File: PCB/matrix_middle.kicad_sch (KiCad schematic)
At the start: 70 parts, among them J12 Conn_02x02_Top_Bottom, J13 Conn_02x02_Top_Bottom, J14 Conn_02x02_Top_Bottom

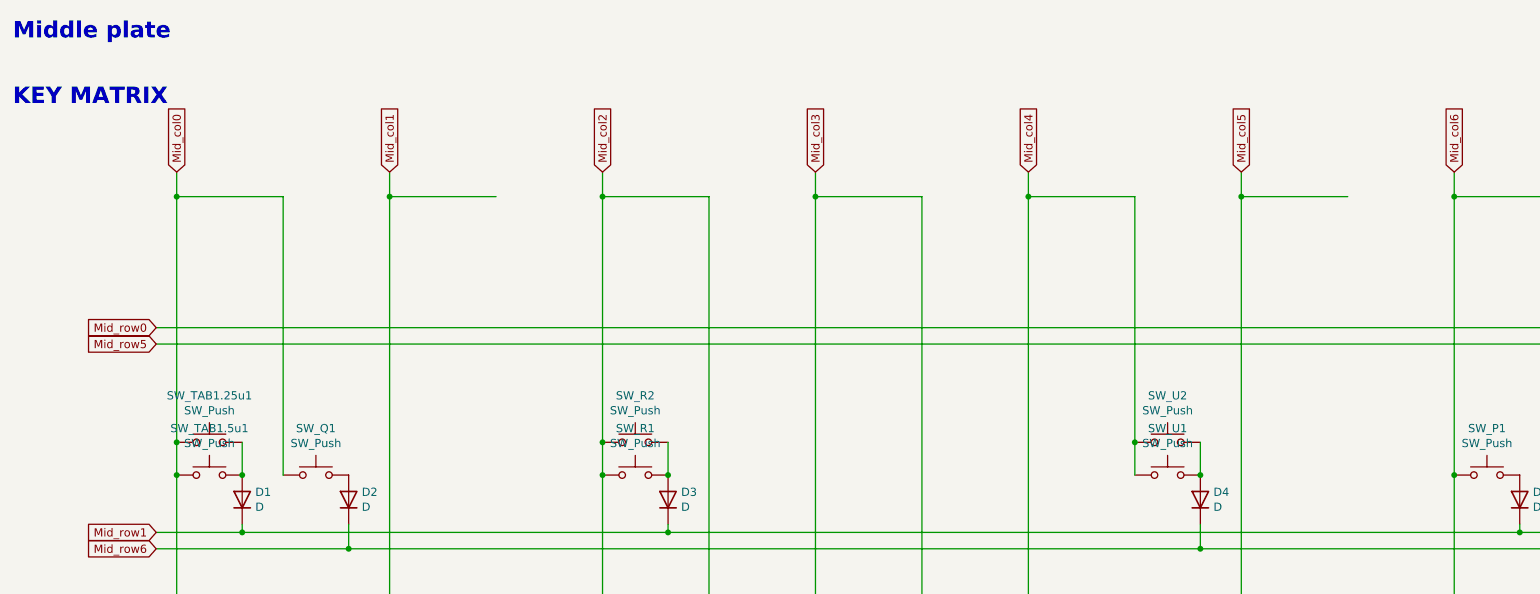
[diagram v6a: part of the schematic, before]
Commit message: スイッチのソケットを廃止
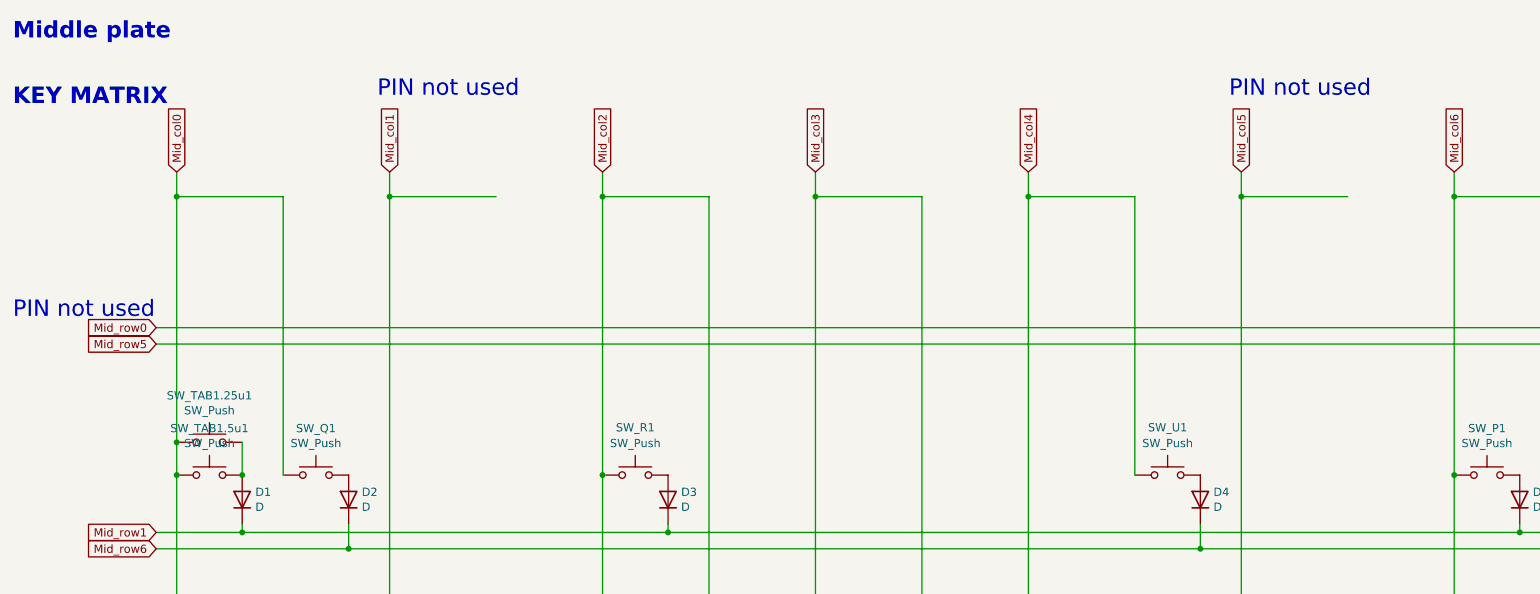
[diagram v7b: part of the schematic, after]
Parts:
- removed SW_R2, SW_U2: SW_Push, MX_Alps_Hybrid:MXOnly-1U-NoLED, symbol Switch:SW_Push
- SW_'1, SW_;2, SW_G1, SW_H1, SW_P1, SW_Q1, SW_R1, SW_R4CenterC1, SW_R4CenterL1, SW_R4CenterR1, SW_U1: footprint MX_Alps_Hybrid:MXOnly-1U-Hotswap-guide -> MX_Alps_Hybrid:MXOnly-1U-NoLED
- SW_BS1.5u1, SW_TAB1.5u1: footprint MX_Alps_Hybrid:MXOnly-1.5U-Hotswap-guide -> MX_Alps_Hybrid:MXOnly-1.5U-NoLED
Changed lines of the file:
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@@
   (junction (at 246.38 93.98) (diameter 0) (color 0 0 0 0)
   )
-  (junction (at 196.85 85.09) (diameter 0) (color 0 0 0 0)
-  )
   (junction (at 211.455 273.05) (diameter 0) (color 0 0 0 0)
   )
-  (junction (at 186.69 80.01) (diameter 0) (color 0 0 0 0)
-  )
   (junction (at 180.34 125.73) (diameter 0) (color 0 0 0 0)
   )
@@
   (junction (at 163.83 160.02) (diameter 0) (color 0 0 0 0)
   )
-  (junction (at 104.14 80.01) (diameter 0) (color 0 0 0 0)
-  )
   (junction (at 236.22 41.91) (diameter 0) (color 0 0 0 0)
   )
@@
   (junction (at 262.89 96.52) (diameter 0) (color 0 0 0 0)
   )
-  (junction (at 114.3 85.09) (diameter 0) (color 0 0 0 0)
-  )
   (wire (pts (xy 281.94 213.36) (xy 281.94 193.04))
     (stroke (width 0) (type default) (color 0 0 0 0))
@@
     (stroke (width 0) (type default) (color 0 0 0 0))
   )
-  (wire (pts (xy 104.14 80.01) (xy 104.14 85.09))
-    (stroke (width 0) (type default) (color 0 0 0 0))
-  )
   (wire (pts (xy 279.4 96.52) (xy 262.89 96.52))
     (stroke (width 0) (type default) (color 0 0 0 0))
@@
     (stroke (width 0) (type default) (color 0 0 0 0))
   )
-  (wire (pts (xy 104.14 41.91) (xy 104.14 80.01))
+  (wire (pts (xy 104.14 41.91) (xy 104.14 85.09))
     (stroke (width 0) (type default) (color 0 0 0 0))
   )
@@
     (stroke (width 0) (type default) (color 0 0 0 0))
   )
-  (wire (pts (xy 186.69 41.91) (xy 186.69 80.01))
-    (stroke (width 0) (type default) (color 0 0 0 0))
-  )
   (wire (pts (xy 220.345 247.65) (xy 186.055 247.65))
     (stroke (width 0) (type default) (color 0 0 0 0))
@@
     (stroke (width 0) (type default) (color 0 0 0 0))
   )
-  (wire (pts (xy 196.85 80.01) (xy 196.85 85.09))
-    (stroke (width 0) (type default) (color 0 0 0 0))
-  )
   (wire (pts (xy 64.77 96.52) (xy 196.85 96.52))
     (stroke (width 0) (type default) (color 0 0 0 0))
@@
     (stroke (width 0) (type default) (color 0 0 0 0))
   )
-  (wire (pts (xy 186.69 80.01) (xy 186.69 85.09))
+  (wire (pts (xy 186.69 41.91) (xy 186.69 85.09))
     (stroke (width 0) (type default) (color 0 0 0 0))
   )
@@
     (stroke (width 0) (type default) (color 0 0 0 0))
   )
-  (wire (pts (xy 114.3 80.01) (xy 114.3 85.09))
-    (stroke (width 0) (type default) (color 0 0 0 0))
-  )
   (wire (pts (xy 196.85 96.52) (xy 262.89 96.52))
     (stroke (width 0) (type default) (color 0 0 0 0))
@@
   (wire (pts (xy 71.12 38.1) (xy 71.12 41.91))
     (stroke (width 0) (type default) (color 0 0 0 0))
+  )
+  (text "PIN not used" (at 69.215 26.67 0)
+    (effects (font (size 2.54 2.54)) (justify left bottom))
   )
   (text "5-way navigation switch" (at 228.6 177.8 0)
@@
     (effects (font (size 2.54 2.54)) (justify left bottom))
   )
+  (text "PIN not used" (at 201.295 26.67 0)
+    (effects (font (size 2.54 2.54)) (justify left bottom))
+  )
   (text "Bottom to Mid: require 12 pins" (at 21.59 222.25 0)
     (effects (font (size 5.08 5.08) (thickness 1.016) bold) (justify left bottom))
@@
   (text "SCREWS to Bottom" (at 187.96 231.14 0)
     (effects (font (size 2.54 2.54) (thickness 0.508) bold) (justify left bottom))
+  )
+  (text "PIN not used" (at 12.7 60.96 0)
+    (effects (font (size 2.54 2.54)) (justify left bottom))
   )
   (global_label "Mid_col5" (shape input) (at 203.2 38.1 90) (fields_autoplaced)
@@
     (pin "1")
   )
-  (symbol (lib_id "Switch:SW_Push") (at 109.22 80.01 0) (unit 1)
-    (in_bom yes) (on_board yes)
-    (property "Reference" "SW_R2" (id 0) (at 109.22 72.771 0))
-    (property "Value" "SW_Push" (id 1) (at 109.22 75.0824 0))
-    (property "Footprint" "MX_Alps_Hybrid:MXOnly-1U-NoLED" (id 2) (at 109.22 74.93 0)
-      (effects (font (size 1.27 1.27)) hide)
-    )
-    (property "Datasheet" "~" (id 3) (at 109.22 74.93 0)
-      (effects (font (size 1.27 1.27)) hide)
-    )
-    (pin "1")
-    (pin "2")
-  )
   (symbol (lib_id "Connector_Generic:Conn_01x01") (at 284.48 128.27 0) (unit 1)
     (in_bom yes) (on_board yes)
@@
   (symbol (lib_id "Switch:SW_Push") (at 191.77 85.09 0) (unit 1)
     (in_bom yes) (on_board yes)
-    (property "Reference" "SW_U1" (id 0) (at 191.77 77.851 0))
+    (property "Reference" "SW_U1" (id 0) (at 191.77 77.724 0))
     (property "Value" "SW_Push" (id 1) (at 191.77 80.1624 0))
-    (property "Footprint" "MX_Alps_Hybrid:MXOnly-1U-Hotswap-guide" (id 2) (at 191.77 80.01 0)
+    (property "Footprint" "MX_Alps_Hybrid:MXOnly-1U-NoLED" (id 2) (at 191.77 80.01 0)
       (effects (font (size 1.27 1.27)) hide)
     )
@@
     (property "Reference" "SW_BS1.5u1" (id 0) (at 257.81 77.851 0))
     (property "Value" "SW_Push" (id 1) (at 257.81 80.1624 0))
-    (property "Footprint" "MX_Alps_Hybrid:MXOnly-1.5U-Hotswap-guide" (id 2) (at 257.81 80.01 0)
+    (property "Footprint" "MX_Alps_Hybrid:MXOnly-1.5U-NoLED" (id 2) (at 257.81 80.01 0)
       (effects (font (size 1.27 1.27)) hide)
     )
@@
     (pin "4")
   )
-  (symbol (lib_id "Switch:SW_Push") (at 191.77 80.01 0) (unit 1)
-    (in_bom yes) (on_board yes)
-    (property "Reference" "SW_U2" (id 0) (at 191.77 72.771 0))
-    (property "Value" "SW_Push" (id 1) (at 191.77 75.0824 0))
-    (property "Footprint" "MX_Alps_Hybrid:MXOnly-1U-NoLED" (id 2) (at 191.77 74.93 0)
-      (effects (font (size 1.27 1.27)) hide)
-    )
-    (property "Datasheet" "~" (id 3) (at 191.77 74.93 0)
-      (effects (font (size 1.27 1.27)) hide)
-    )
-    (pin "1")
-    (pin "2")
-  )
   (symbol (lib_id "Connector_Generic:Conn_01x01") (at 284.48 160.02 0) (unit 1)
     (in_bom yes) (on_board yes)
@@
     (property "Reference" "SW_R4CenterL1" (id 0) (at 142.24 141.351 0))
     (property "Value" "SW_Push" (id 1) (at 142.24 143.6624 0))
-    (property "Footprint" "MX_Alps_Hybrid:MXOnly-1U-Hotswap-guide" (id 2) (at 142.24 143.51 0)
+    (property "Footprint" "MX_Alps_Hybrid:MXOnly-1U-NoLED" (id 2) (at 142.24 143.51 0)
       (effects (font (size 1.27 1.27)) hide)
     )
@@
     (property "Reference" "SW_P1" (id 0) (at 241.3 77.851 0))
     (property "Value" "SW_Push" (id 1) (at 241.3 80.1624 0))
-    (property "Footprint" "MX_Alps_Hybrid:MXOnly-1U-Hotswap-guide" (id 2) (at 241.3 80.01 0)
+    (property "Footprint" "MX_Alps_Hybrid:MXOnly-1U-NoLED" (id 2) (at 241.3 80.01 0)
       (effects (font (size 1.27 1.27)) hide)
     )
@@
     (property "Reference" "SW_G1" (id 0) (at 125.73 109.601 0))
     (property "Value" "SW_Push" (id 1) (at 125.73 111.9124 0))
-    (property "Footprint" "MX_Alps_Hybrid:MXOnly-1U-Hotswap-guide" (id 2) (at 125.73 111.76 0)
+    (property "Footprint" "MX_Alps_Hybrid:MXOnly-1U-NoLED" (id 2) (at 125.73 111.76 0)
       (effects (font (size 1.27 1.27)) hide)
     )
@@
     (property "Reference" "SW_Q1" (id 0) (at 59.69 77.851 0))
     (property "Value" "SW_Push" (id 1) (at 59.69 80.1624 0))
-    (property "Footprint" "MX_Alps_Hybrid:MXOnly-1U-Hotswap-guide" (id 2) (at 59.69 80.01 0)
+    (property "Footprint" "MX_Alps_Hybrid:MXOnly-1U-NoLED" (id 2) (at 59.69 80.01 0)
       (effects (font (size 1.27 1.27)) hide)
     )
@@
   (symbol (lib_id "Switch:SW_Push") (at 109.22 85.09 0) (unit 1)
     (in_bom yes) (on_board yes)
-    (property "Reference" "SW_R1" (id 0) (at 109.22 77.851 0))
+    (property "Reference" "SW_R1" (id 0) (at 109.22 77.724 0))
     (property "Value" "SW_Push" (id 1) (at 109.22 80.1624 0))
-    (property "Footprint" "MX_Alps_Hybrid:MXOnly-1U-Hotswap-guide" (id 2) (at 109.22 80.01 0)
+    (property "Footprint" "MX_Alps_Hybrid:MXOnly-1U-NoLED" (id 2) (at 109.22 80.01 0)
       (effects (font (size 1.27 1.27)) hide)
     )
@@
     (property "Reference" "SW_;2" (id 0) (at 142.24 109.601 0))
     (property "Value" "SW_Push" (id 1) (at 142.24 111.9124 0))
-    (property "Footprint" "MX_Alps_Hybrid:MXOnly-1U-Hotswap-guide" (id 2) (at 142.24 111.76 0)
+    (property "Footprint" "MX_Alps_Hybrid:MXOnly-1U-NoLED" (id 2) (at 142.24 111.76 0)
       (effects (font (size 1.27 1.27)) hide)
     )
@@
     (property "Reference" "SW_'1" (id 0) (at 158.75 109.601 0))
     (property "Value" "SW_Push" (id 1) (at 158.75 111.9124 0))
-    (property "Footprint" "MX_Alps_Hybrid:MXOnly-1U-Hotswap-guide" (id 2) (at 158.75 111.76 0)
+    (property "Footprint" "MX_Alps_Hybrid:MXOnly-1U-NoLED" (id 2) (at 158.75 111.76 0)
       (effects (font (size 1.27 1.27)) hide)
     )
@@
     (property "Reference" "SW_R4CenterR1" (id 0) (at 175.26 141.351 0))
     (property "Value" "SW_Push" (id 1) (at 175.26 143.6624 0))
-    (property "Footprint" "MX_Alps_Hybrid:MXOnly-1U-Hotswap-guide" (id 2) (at 175.26 143.51 0)
+    (property "Footprint" "MX_Alps_Hybrid:MXOnly-1U-NoLED" (id 2) (at 175.26 143.51 0)
       (effects (font (size 1.27 1.27)) hide)
     )
@@
     (property "Reference" "SW_R4CenterC1" (id 0) (at 158.75 141.351 0))
     (property "Value" "SW_Push" (id 1) (at 158.75 143.6624 0))
-    (property "Footprint" "MX_Alps_Hybrid:MXOnly-1U-Hotswap-guide" (id 2) (at 158.75 143.51 0)
+    (property "Footprint" "MX_Alps_Hybrid:MXOnly-1U-NoLED" (id 2) (at 158.75 143.51 0)
       (effects (font (size 1.27 1.27)) hide)
     )
@@
     (property "Reference" "SW_H1" (id 0) (at 175.26 109.601 0))
     (property "Value" "SW_Push" (id 1) (at 175.26 111.9124 0))
-    (property "Footprint" "MX_Alps_Hybrid:MXOnly-1U-Hotswap-guide" (id 2) (at 175.26 111.76 0)
+    (property "Footprint" "MX_Alps_Hybrid:MXOnly-1U-NoLED" (id 2) (at 175.26 111.76 0)
       (effects (font (size 1.27 1.27)) hide)
     )
@@
     (property "Reference" "SW_TAB1.5u1" (id 0) (at 43.18 77.851 0))
     (property "Value" "SW_Push" (id 1) (at 43.18 80.1624 0))
-    (property "Footprint" "MX_Alps_Hybrid:MXOnly-1.5U-Hotswap-guide" (id 2) (at 43.18 80.01 0)
-      (effects (font (size 1.27 1.27)) hide)
-    )
+    (property "Footprint" "MX_Alps_Hybrid:MXOnly-1.5U-NoLED" (id 2) (at 43.18 80.01 0)
+      (effects (font (size 1.27 1.27)) hide)
+    )
